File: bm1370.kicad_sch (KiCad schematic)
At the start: 44 parts, among them U5 MCP1824T-1202E/OT, U6 MCP1824T-0802E, U7 25MHz, U8 BM1370_mode1, U9 SN74AVC4T774

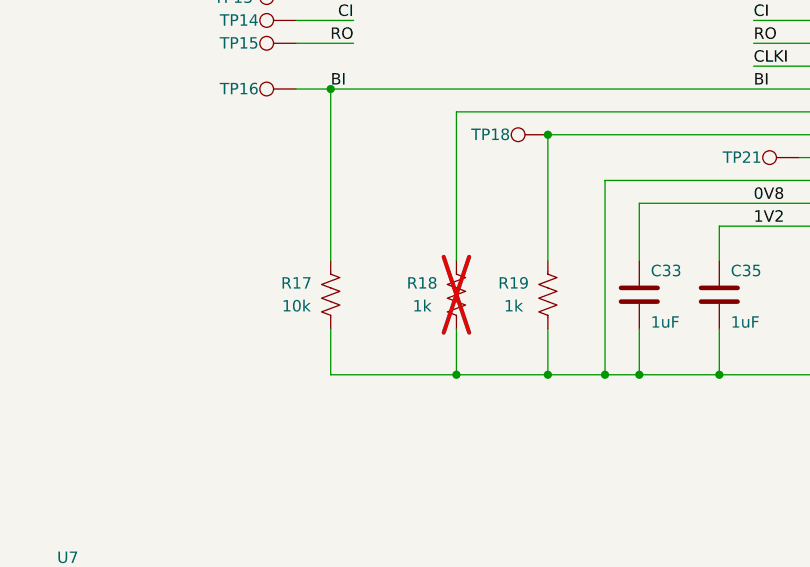
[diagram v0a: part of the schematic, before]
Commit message: Revert "added pullup resistors for #25"
This reverts commit 91572af801fdd590416a5d3df79444bb16faa4cf.
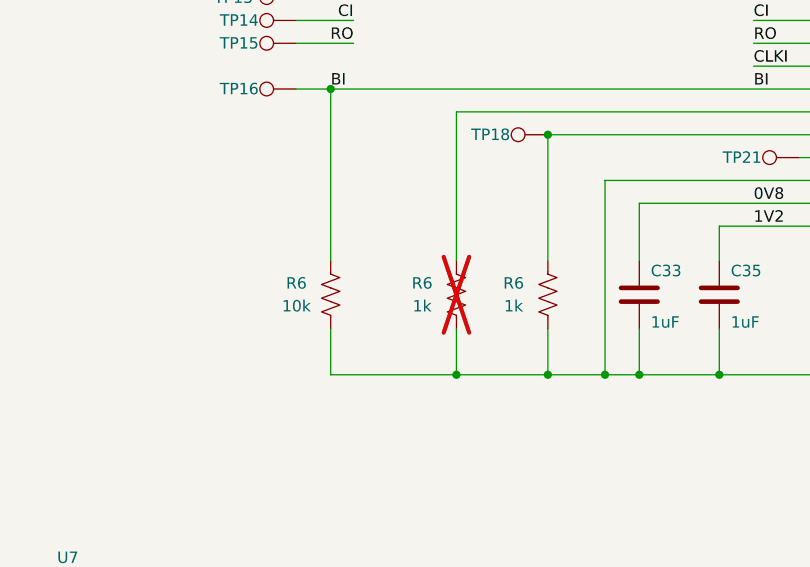
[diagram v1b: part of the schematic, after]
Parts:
- renumbered R18 to R6, R19 to R6, R17 to R6
